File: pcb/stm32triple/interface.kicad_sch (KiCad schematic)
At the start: 26 parts, among them J2 Term, P1 har-flexicon 2,54 MSH-4, P2 WAGO2061-602, U3 SP3485CN

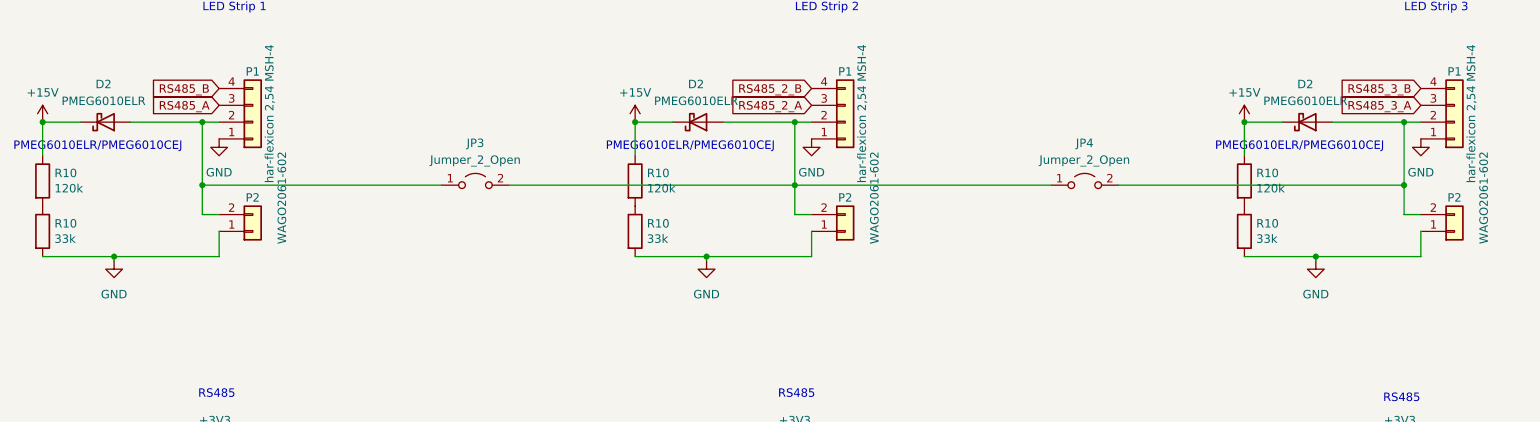
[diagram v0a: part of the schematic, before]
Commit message: Add IR receiver
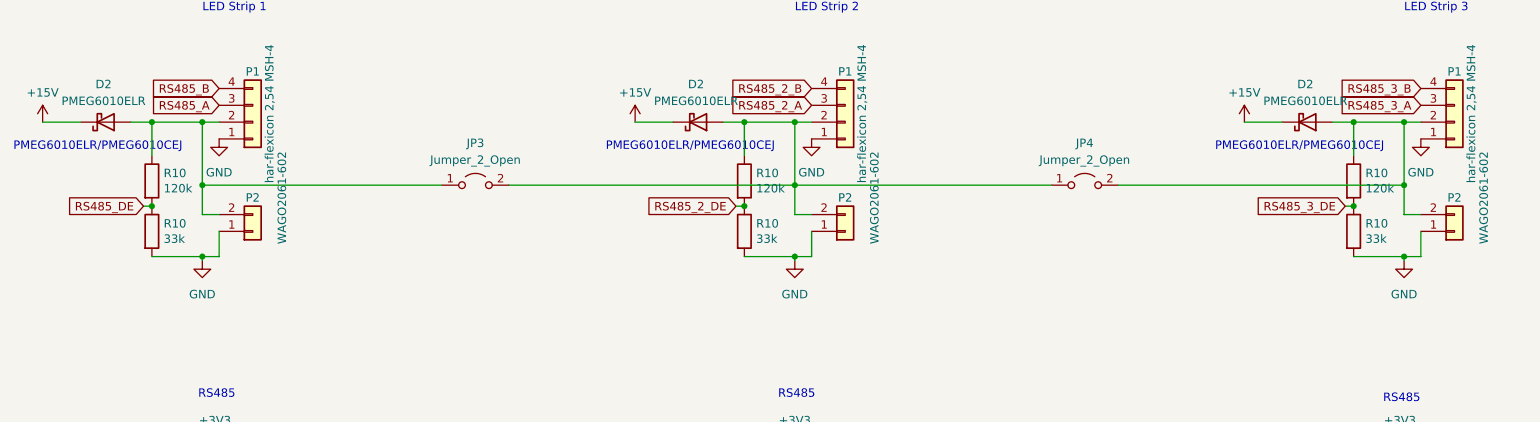
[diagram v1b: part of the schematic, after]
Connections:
- net +15V: no longer R10.1, R10.1, R10.1
- net RS485_2_DE: now also R10.1, R10.2
- net RS485_3_DE: now also R10.1, R10.2
- net RS485_DE: now also R10.1, R10.2
- net at D2.2 (A), JP3.2 (B), JP4.1 (A)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: now also R10.1
- net at D2.2 (A), JP4.2 (B), P1.2 (Pin_2)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: now also R10.1
- net at D2.2 (A), JP3.1 (A), P1.2 (Pin_2)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: now also R10.1
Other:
- moved on the sheet: R10

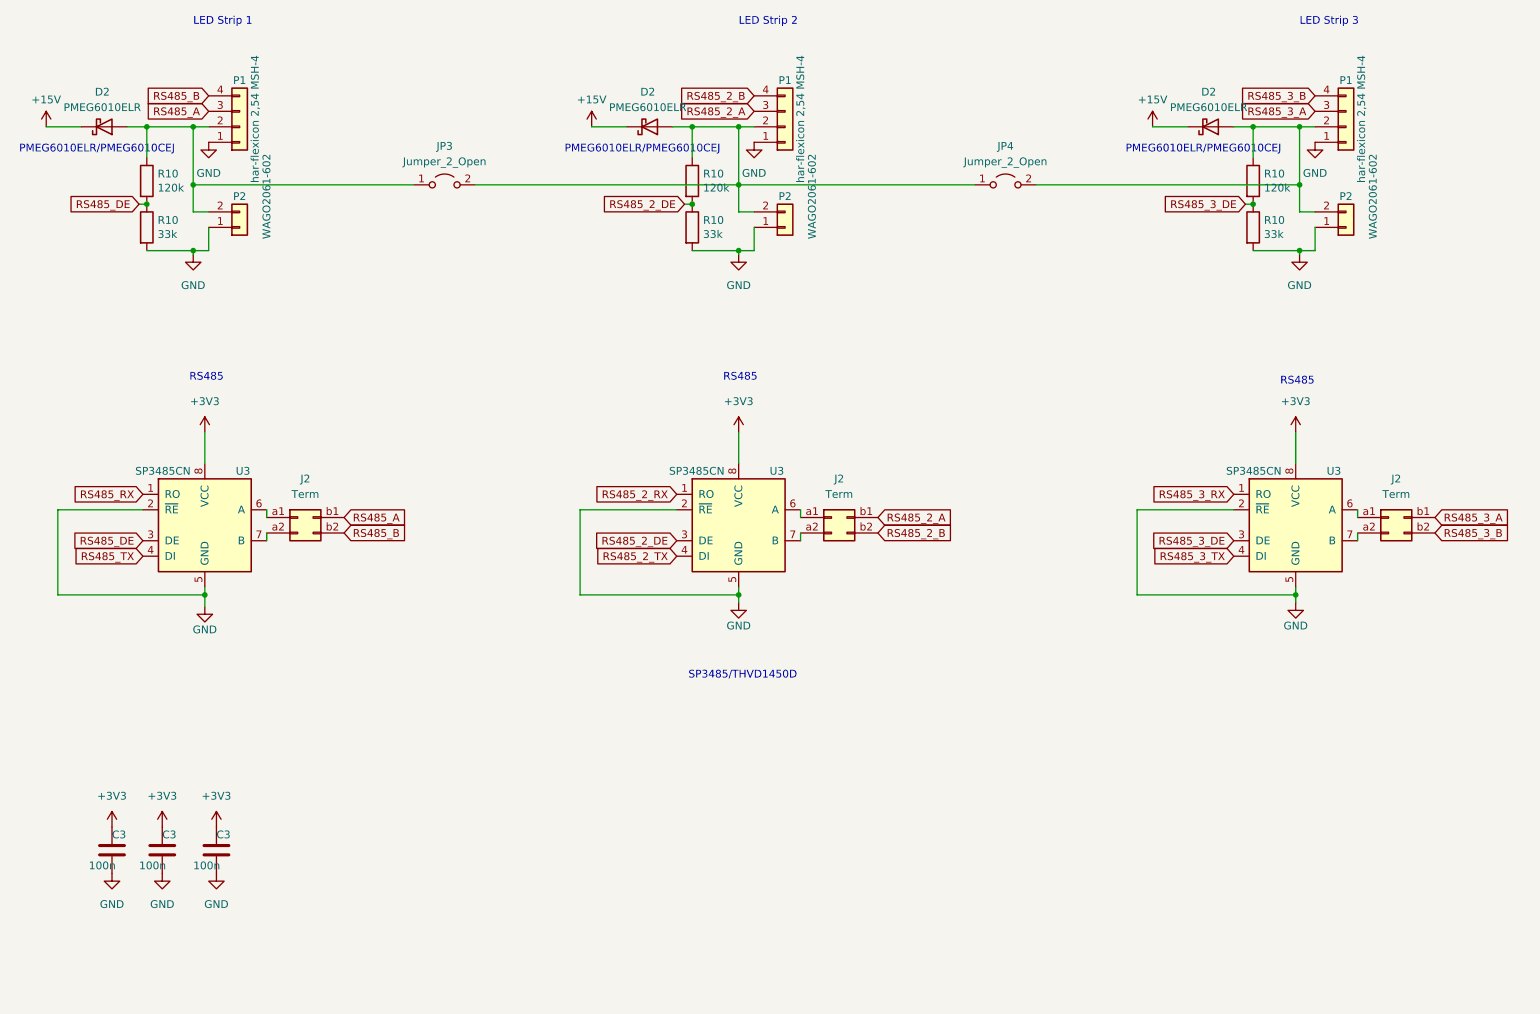
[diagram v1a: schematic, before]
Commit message: Control brightness and duraton with remote control
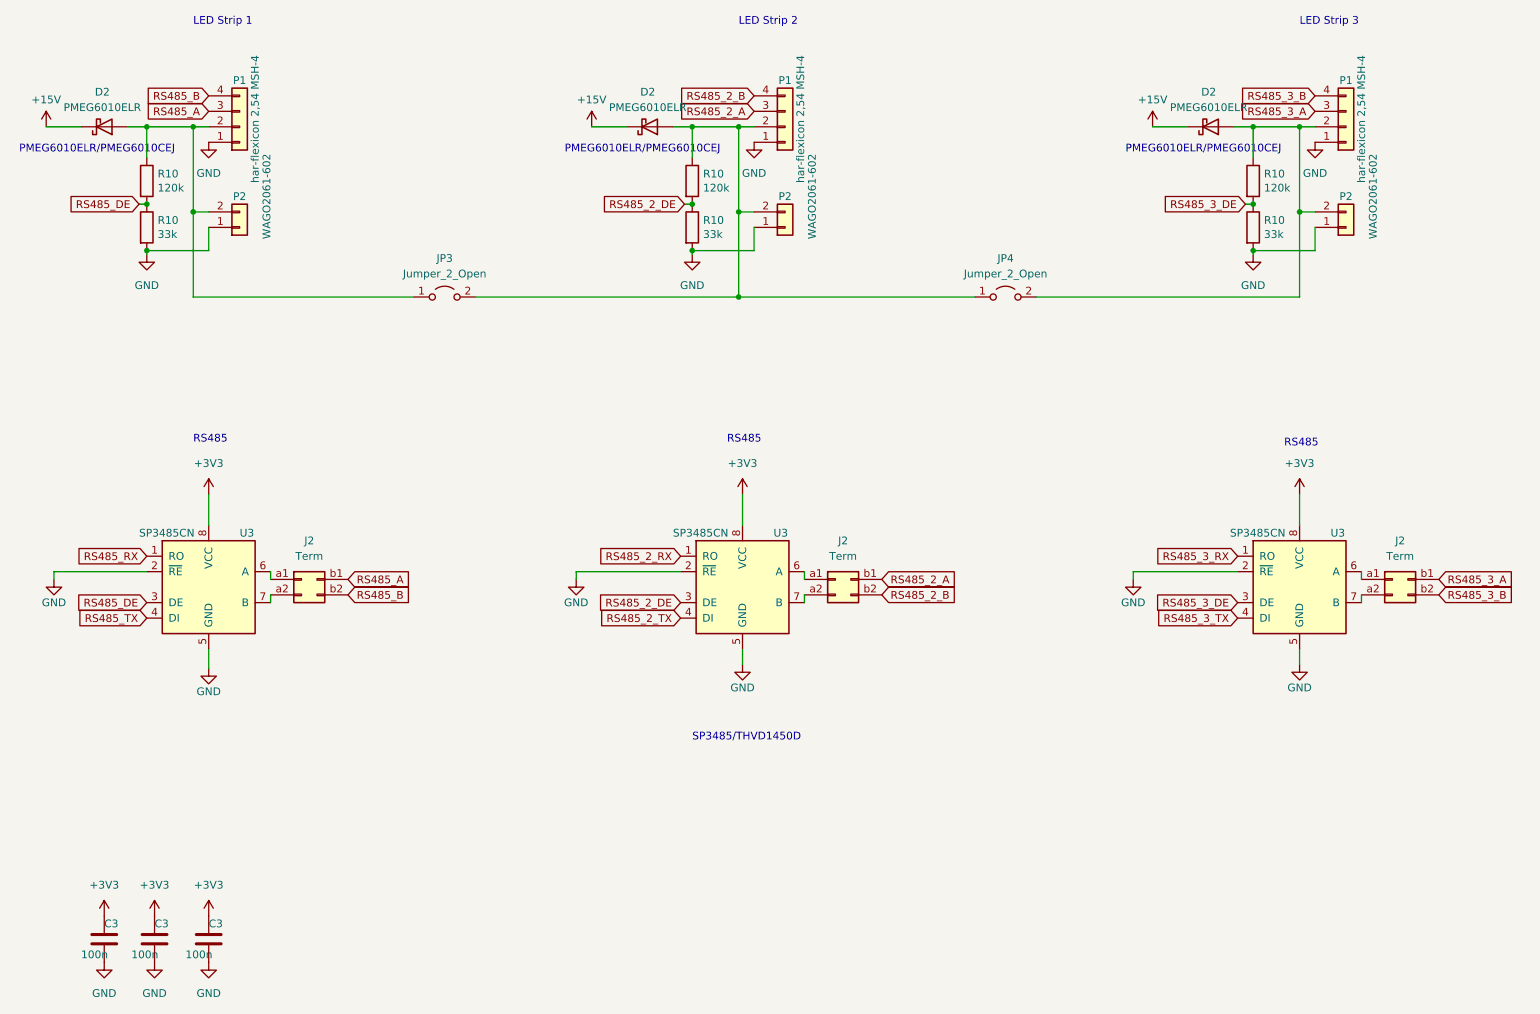
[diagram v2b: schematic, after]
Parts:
- U3: footprint local:SP3485 -> local:SO-8
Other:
- moved on the sheet: C3, J2, JP3, JP4, U3

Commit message: Add SnowSparkle, new footprints
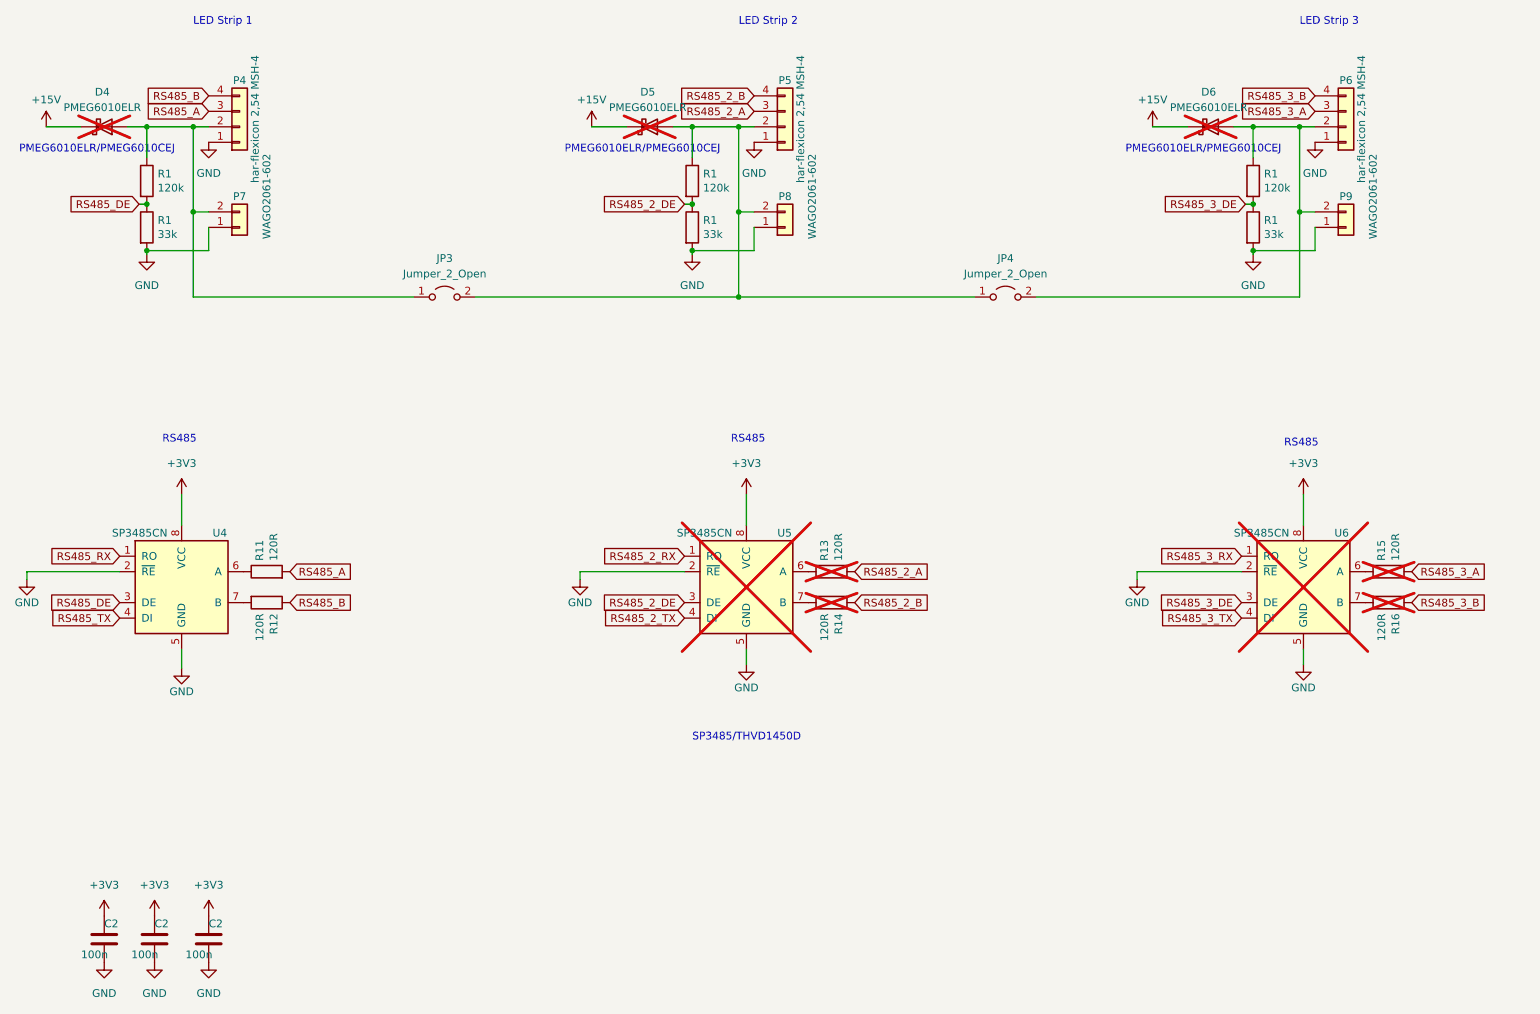
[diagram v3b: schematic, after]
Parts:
- removed J2 (x3): Term, local:Termination, symbol Connector_Generic:Conn_02x02_Row_Letter_First
- added R11, R12, R13, R14, R15, R16: 120R, local:1206-term, symbol Device:R
- C2: renamed from C3; footprint Capacitor_SMD:C_0603_1608Metric -> local:0603
- D4, D5, D6: renamed from D2; now not fitted
- JP3, JP4: now left out of the parts list
- P4, P5, P6: renamed from P1; now left out of the parts list
- P7, P8, P9: renamed from P2; now left out of the parts list
- R1: renamed from R10; footprint Resistor_SMD:R_0603_1608Metric -> local:0603
- U5, U6: renamed from U3; now not fitted
- renumbered U3 to U4
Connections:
- net RS485_2_A: now also R13.2
- net RS485_2_B: now also R14.1
- net RS485_3_A: now also R15.2
- net RS485_3_B: now also R16.1
- net RS485_A: now also R11.2
- net RS485_B: now also R12.1
- net at U4.6 (A): now also R11.1
- net at U4.7 (B): now also R12.2
- net at U5.6 (A): now also R13.1
- net at U5.7 (B): now also R14.2
- net at U6.6 (A): now also R15.1
- net at U6.7 (B): now also R16.2
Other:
- moved on the sheet: U4
